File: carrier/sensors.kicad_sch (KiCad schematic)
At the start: 39 parts, among them J10 Conn_01x08, J8 Conn_02x16_Top_Bottom, J9 Conn_01x04, U11 BME680, U12 BMI088, U13 MMC5603NJ, U14 PCA9685PW

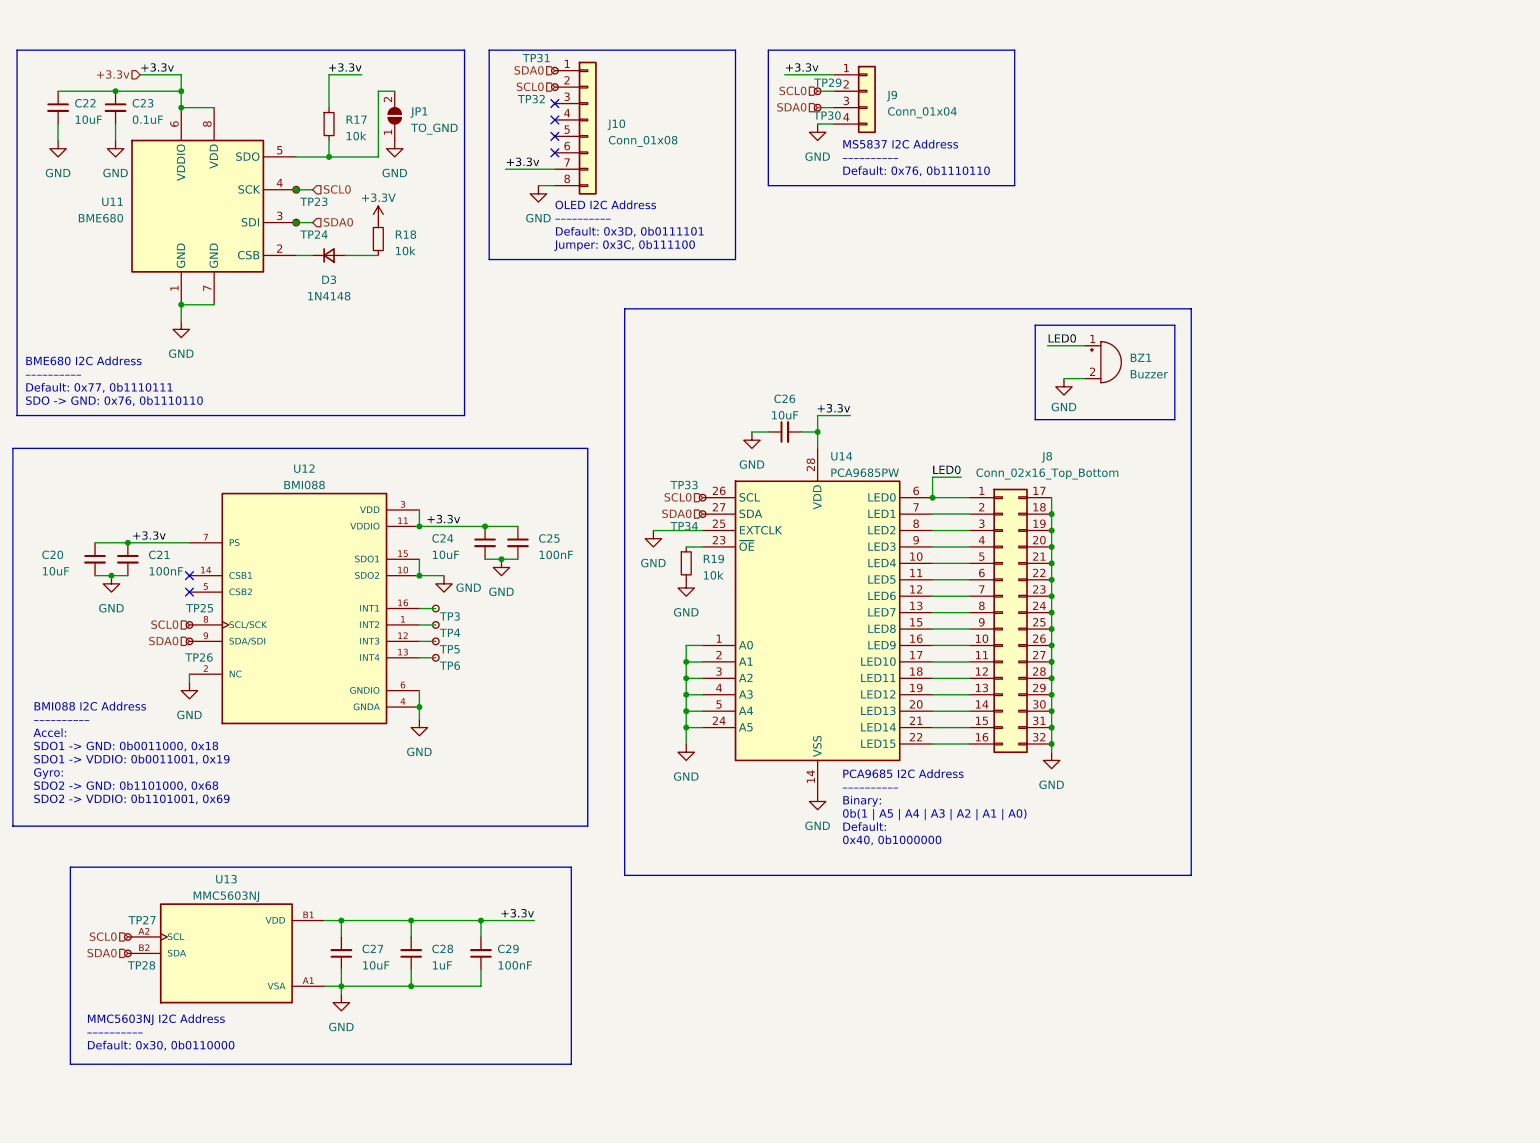
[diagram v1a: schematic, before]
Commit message: Feat: more routing (gpio and i2c)
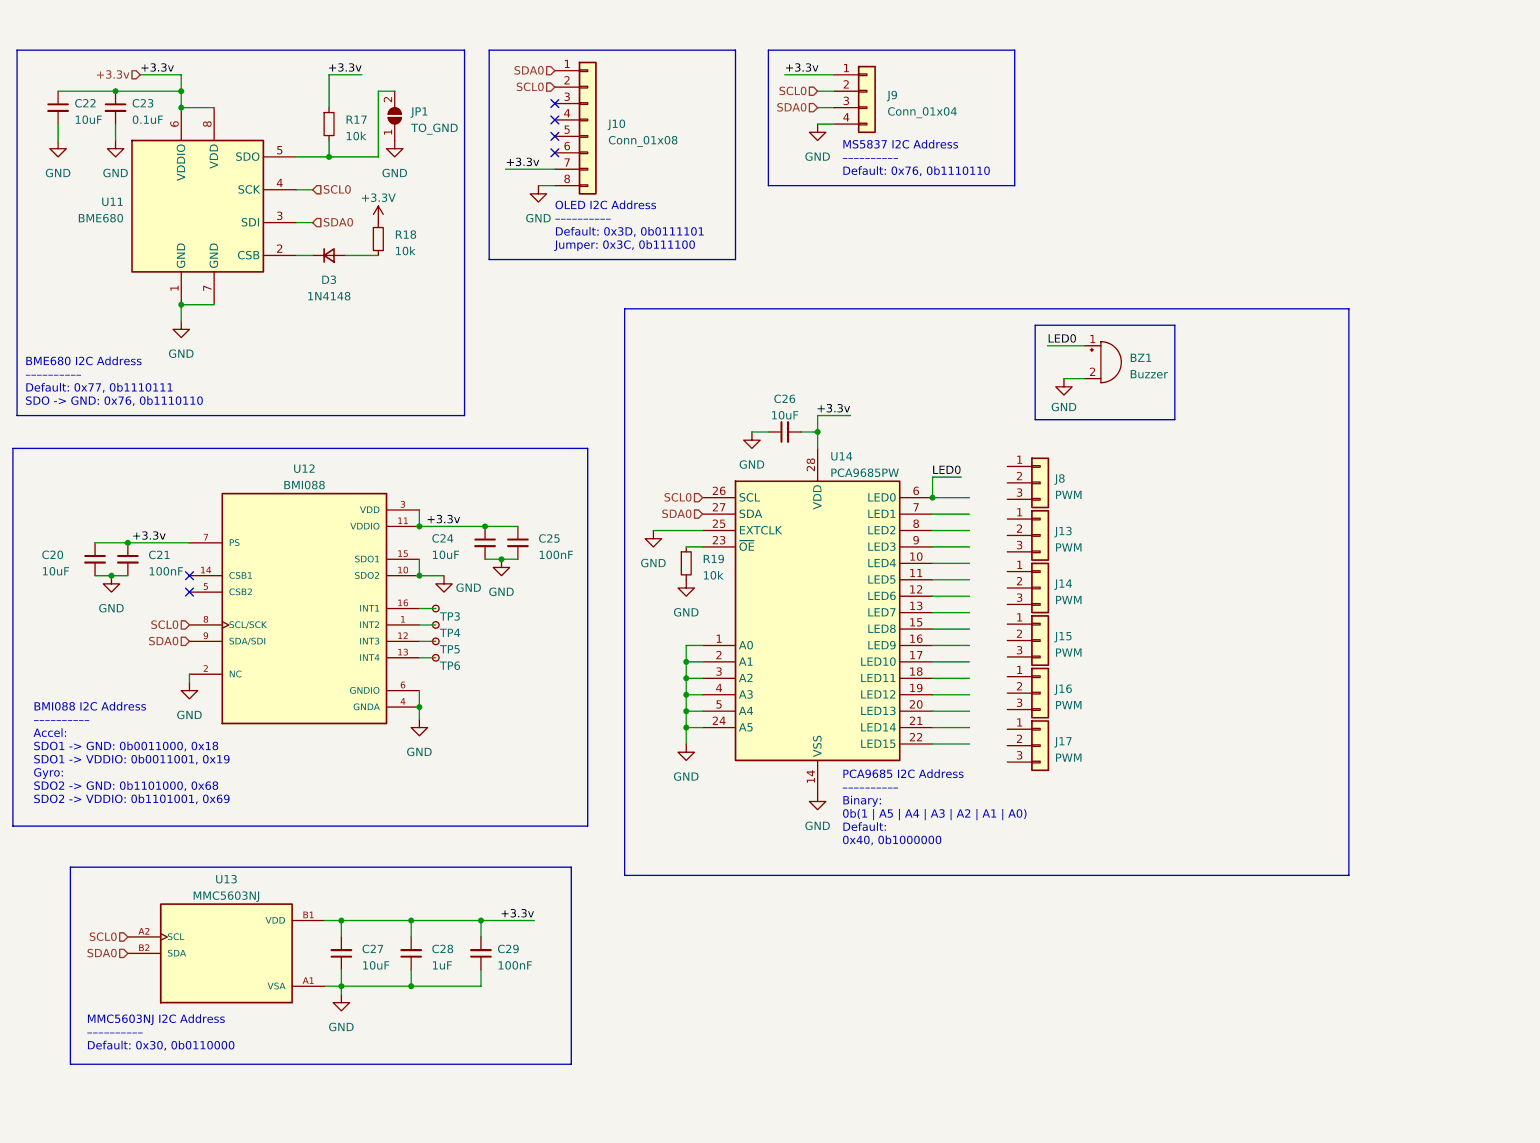
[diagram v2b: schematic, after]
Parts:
- removed J8: Conn_02x16_Top_Bottom, Connector_PinHeader_2.54mm:PinHeader_2x16_P2.54mm_Vertical, symbol Connector_Generic:Conn_02x16_Top_Bottom
- removed TP23, TP24, TP25, TP26, TP27, TP28, TP29, TP30, TP31, TP32, TP33, TP34: ~, TestPoint:TestPoint_Pad_D1.5mm, symbol Connector:TestPoint_Small
- added J13, J14, J15, J16, J17, J8: PWM, symbol Connector_Generic:Conn_01x03

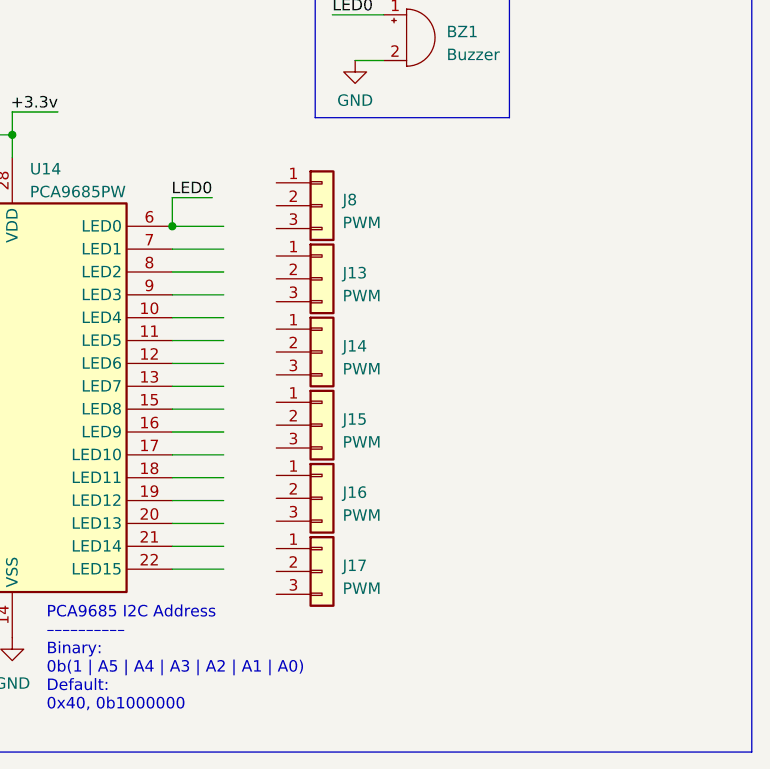
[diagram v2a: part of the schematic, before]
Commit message: Feat: more routing with i2c and gpio
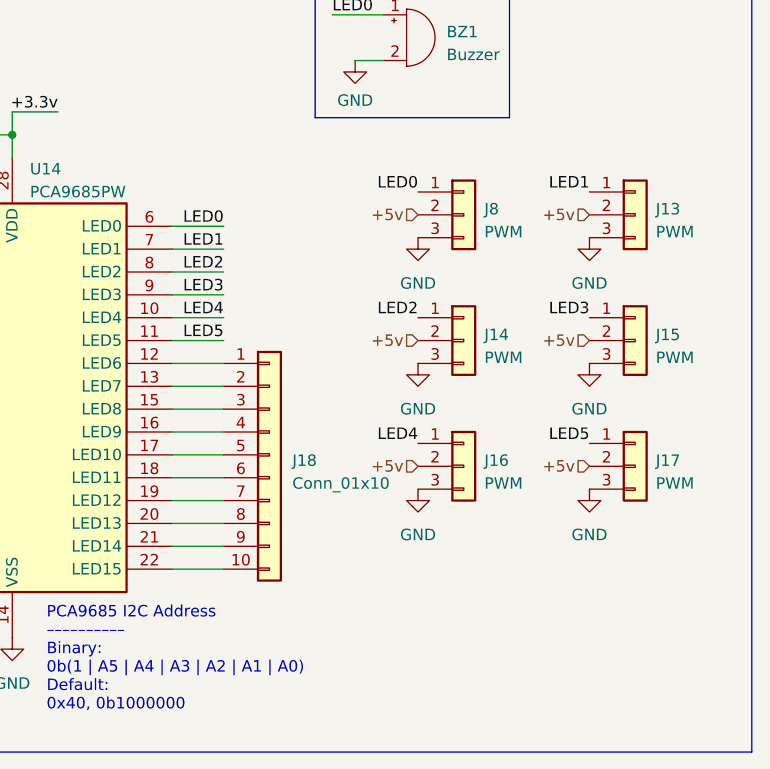
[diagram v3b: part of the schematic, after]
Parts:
- added J18: Conn_01x10, Connector_Molex:Molex_PicoBlade_53047-1010_1x10_P1.25mm_Vertical, symbol Connector_Generic:Conn_01x10
- J13, J14, J15, J16, J17, J8: footprint (none) -> Connector_PinHeader_2.54mm:PinHeader_1x03_P2.54mm_Vertical
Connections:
- net GND: now also J13.3 (Pin_3), J14.3 (Pin_3), J15.3 (Pin_3), J16.3 (Pin_3), J17.3 (Pin_3), J8.3 (Pin_3)
- net LED0: now also J8.1 (Pin_1)
- net LED3: now reaches J15.1 (Pin_1)
- net LED3: now also U14.9 (LED3)
- net +5v: now reaches J15.2 (Pin_2)
- net +5v: now also J13.2 (Pin_2), J14.2 (Pin_2), J16.2 (Pin_2), J17.2 (Pin_2), J8.2 (Pin_2)
- net LED1: now reaches J13.1 (Pin_1)
- net LED1: now also U14.7 (LED1)
- net LED2: now reaches J14.1 (Pin_1)
- net LED2: now also U14.8 (LED2)
- net LED4: now reaches J16.1 (Pin_1)
- net LED4: now also U14.10 (LED4)
- net LED5: now reaches J17.1 (Pin_1)
- net LED5: now also U14.11 (LED5)
- net at U14.12 (LED6): now also J18.1 (Pin_1)
- net at U14.13 (LED7): now also J18.2 (Pin_2)
- net at U14.15 (LED8): now also J18.3 (Pin_3)
- net at U14.16 (LED9): now also J18.4 (Pin_4)
- net at U14.17 (LED10): now also J18.5 (Pin_5)
- net at U14.18 (LED11): now also J18.6 (Pin_6)
- net at U14.19 (LED12): now also J18.7 (Pin_7)
- net at U14.20 (LED13): now also J18.8 (Pin_8)
- net at U14.21 (LED14): now also J18.9 (Pin_9)
- net at U14.22 (LED15): now also J18.10 (Pin_10)
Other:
- moved on the sheet: J13, J14, J15, J16, J17, J8

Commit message: feat: carrier board layout v2
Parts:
- removed J10: Conn_01x08, Connector_PinHeader_2.54mm:PinHeader_1x08_P2.54mm_Vertical, symbol Connector_Generic:Conn_01x08
- added J6: Conn_01x04, Connector_PinHeader_2.54mm:PinHeader_1x04_P2.54mm_Vertical, symbol Connector_Generic:Conn_01x04
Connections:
- net +3.3v: now also J6.3 (Pin_3)
- net GND: now also J6.4 (Pin_4)
- net SCL0: now also J6.2 (Pin_2)
- net SDA0: now also J6.1 (Pin_1)
- no-connect marks 6 -> 2
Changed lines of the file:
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@@
   )
   (no_connect (at 77.47 103.505))
-  (no_connect (at 133.985 27.94))
-  (no_connect (at 133.985 33.02))
-  (no_connect (at 133.985 30.48))
-  (no_connect (at 133.985 35.56))
   (no_connect (at 77.47 100.965))
   (wire (pts (xy 154.305 121.92) (xy 156.845 121.92))
@@
     (stroke (width 0) (type default))
   )
-  (wire (pts (xy 131.445 40.64) (xy 133.985 40.64))
+  (wire (pts (xy 135.128 34.544) (xy 137.668 34.544))
     (stroke (width 0) (type default))
   )
@@
     (stroke (width 0) (type default))
   )
-  (wire (pts (xy 126.365 38.1) (xy 133.985 38.1))
+  (wire (pts (xy 130.048 32.004) (xy 137.668 32.004))
     (stroke (width 0) (type default))
   )
@@
     (effects (font (size 1.27 1.27)) (justify right bottom))
   )
-  (label "+3.3v" (at 126.365 38.1 0) (fields_autoplaced)
+  (label "+3.3v" (at 130.048 32.004 0) (fields_autoplaced)
     (effects (font (size 1.27 1.27)) (justify left bottom))
   )
@@
     (effects (font (size 1.27 1.27)) (justify right bottom))
   )
-  (hierarchical_label "SDA0" (shape input) (at 133.985 22.86 180) (fields_autoplaced)
+  (hierarchical_label "SDA0" (shape input) (at 137.668 26.924 180) (fields_autoplaced)
     (effects (font (size 1.27 1.27)) (justify right))
   )
@@
     (effects (font (size 1.27 1.27)) (justify right))
   )
-  (hierarchical_label "SCL0" (shape input) (at 133.985 25.4 180) (fields_autoplaced)
-    (effects (font (size 1.27 1.27)) (justify right))
-  )
-  (symbol (lib_id "power:GND") (at 131.445 40.64 0) (unit 1)
-    (in_bom yes) (on_board yes) (dnp no) (fields_autoplaced)
-    (property "Reference" "#PWR062" (at 131.445 46.99 0)
-      (effects (font (size 1.27 1.27)) hide)
-    )
-    (property "Value" "GND" (at 131.445 45.72 0)
-      (effects (font (size 1.27 1.27)))
-    )
-    (property "Footprint" "" (at 131.445 40.64 0)
-      (effects (font (size 1.27 1.27)) hide)
-    )
-    (property "Datasheet" "" (at 131.445 40.64 0)
+  (hierarchical_label "SCL0" (shape input) (at 137.668 29.464 180) (fields_autoplaced)
+    (effects (font (size 1.27 1.27)) (justify right))
+  )
+  (symbol (lib_id "power:GND") (at 135.128 34.544 0) (unit 1)
+    (in_bom yes) (on_board yes) (dnp no) (fields_autoplaced)
+    (property "Reference" "#PWR062" (at 135.128 40.894 0)
+      (effects (font (size 1.27 1.27)) hide)
+    )
+    (property "Value" "GND" (at 135.128 39.624 0)
+      (effects (font (size 1.27 1.27)))
+    )
+    (property "Footprint" "" (at 135.128 34.544 0)
+      (effects (font (size 1.27 1.27)) hide)
+    )
+    (property "Datasheet" "" (at 135.128 34.544 0)
       (effects (font (size 1.27 1.27)) hide)
     )
@@
     )
   )
+  (symbol (lib_id "Connector_Generic:Conn_01x04") (at 142.748 29.464 0) (unit 1)
+    (in_bom yes) (on_board yes) (dnp no) (fields_autoplaced)
+    (property "Reference" "J6" (at 145.288 30.099 0)
+      (effects (font (size 1.27 1.27)) (justify left))
+    )
+    (property "Value" "Conn_01x04" (at 145.288 32.639 0)
+      (effects (font (size 1.27 1.27)) (justify left))
+    )
+    (property "Footprint" "Connector_PinHeader_2.54mm:PinHeader_1x04_P2.54mm_Vertical" (at 142.748 29.464 0)
+      (effects (font (size 1.27 1.27)) hide)
+    )
+    (property "Datasheet" "~" (at 142.748 29.464 0)
+      (effects (font (size 1.27 1.27)) hide)
+    )
+    (pin "1")
+    (pin "2")
+    (pin "3")
+    (pin "4")
+    (instances
+      (project "carrier"
+        (path "/4b1cea9d-93bc-4380-88c3-ede99bb53de2/982f4b68-a38c-4772-af6b-ffe8049f8a46"
+          (reference "J6") (unit 1)
+        )
+      )
+    )
+  )
   (symbol (lib_id "Device:C_Small") (at 66.04 28.575 0) (unit 1)
     (in_bom yes) (on_board yes) (dnp no) (fields_autoplaced)
@@
         )
       )
-    )
-  )
-  (symbol (lib_id "Connector_Generic:Conn_01x08") (at 139.065 30.48 0) (unit 1)
-    (in_bom yes) (on_board yes) (dnp no) (fields_autoplaced)
-    (property "Reference" "J10" (at 142.24 31.115 0)
-      (effects (font (size 1.27 1.27)) (justify left))
-    )
-    (property "Value" "Conn_01x08" (at 142.24 33.655 0)
-      (effects (font (size 1.27 1.27)) (justify left))
-    )
-    (property "Footprint" "Connector_PinHeader_2.54mm:PinHeader_1x08_P2.54mm_Vertical" (at 139.065 30.48 0)
-      (effects (font (size 1.27 1.27)) hide)
-    )
-    (property "Datasheet" "~" (at 139.065 30.48 0)
-      (effects (font (size 1.27 1.27)) hide)
-    )
-    (pin "1")
-    (pin "2")
-    (pin "3")
-    (pin "4")
-    (pin "5")
-    (pin "6")
-    (pin "7")
-    (pin "8")
-    (instances
-      (project "carrier"
-        (path "/4b1cea9d-93bc-4380-88c3-ede99bb53de2/982f4b68-a38c-4772-af6b-ffe8049f8a46"
-          (reference "J10") (unit 1)
-        )
-      )

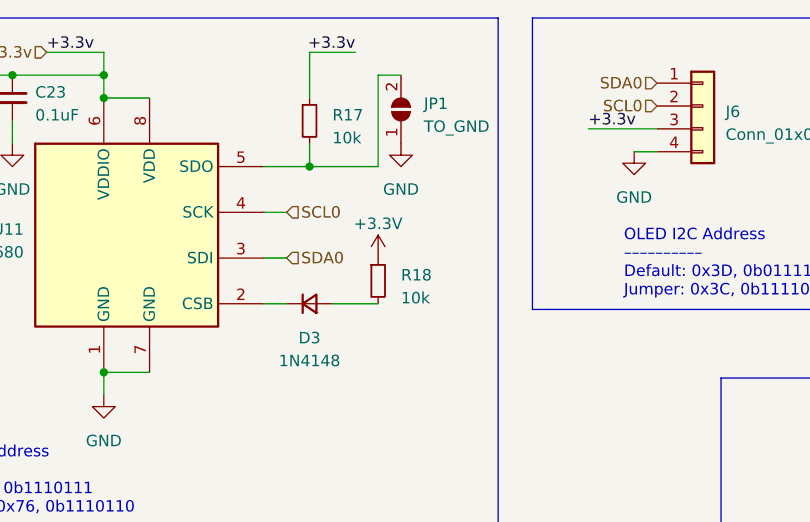
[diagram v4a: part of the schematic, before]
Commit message: Feat: most routes on i2c side and power complete
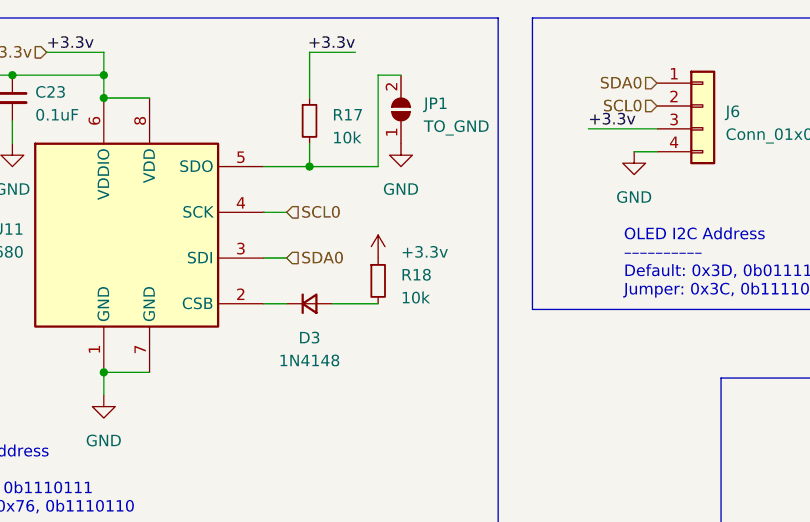
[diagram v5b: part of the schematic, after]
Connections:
- net +3.3V is gone; now on net +3.3v: R18.1
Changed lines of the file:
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@@
       (effects (font (size 1.27 1.27)) hide)
     )
-    (property "Value" "+3.3V" (at 106.68 42.545 0)
-      (effects (font (size 1.27 1.27)))
+    (property "Value" "+3.3v" (at 109.22 45.72 0)
+      (effects (font (size 1.27 1.27)) (justify left))
     )
     (property "Footprint" "" (at 106.68 46.355 0)

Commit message: Feat: semi-baked adc implementation
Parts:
- added C37: 10uF, symbol Device:C_Small
- added C38: 0.1uF, symbol Device:C_Small
- added FB1: Ferrite, symbol Device:FerriteBead_Small
- added J21: AIN, Connector_PinHeader_2.54mm:PinHeader_1x04_P2.54mm_Vertical, symbol Connector_Generic:Conn_01x04
- added R21, R22: 10k, symbol Device:R_Small
- added U16: ADS1015IDGS, Package_SO:TSSOP-10_3x3mm_P0.5mm, symbol Analog_ADC:ADS1015IDGS
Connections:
- net GND: now also R22.2, U16.3 (GND)
- net SCL0: now also U16.9 (SDA)
- net SDA0: now also U16.10 (SCL)
- new net: R22.1, U16.1 (ADDR)
- new net: J21.1 (Pin_1), U16.7 (AIN3)
- new net: J21.2 (Pin_2), U16.6 (AIN2)
- new net: J21.3 (Pin_3), U16.5 (AIN1)
- new net: J21.4 (Pin_4), U16.4 (AIN0)
- new net: R21.2, U16.2 (ALERT/RDY)
